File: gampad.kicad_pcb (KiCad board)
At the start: 2 copper layers, 18 parts, among them J1 swd header, U1 STM32L442KCUx, U2 MIC5504-3.3YM5

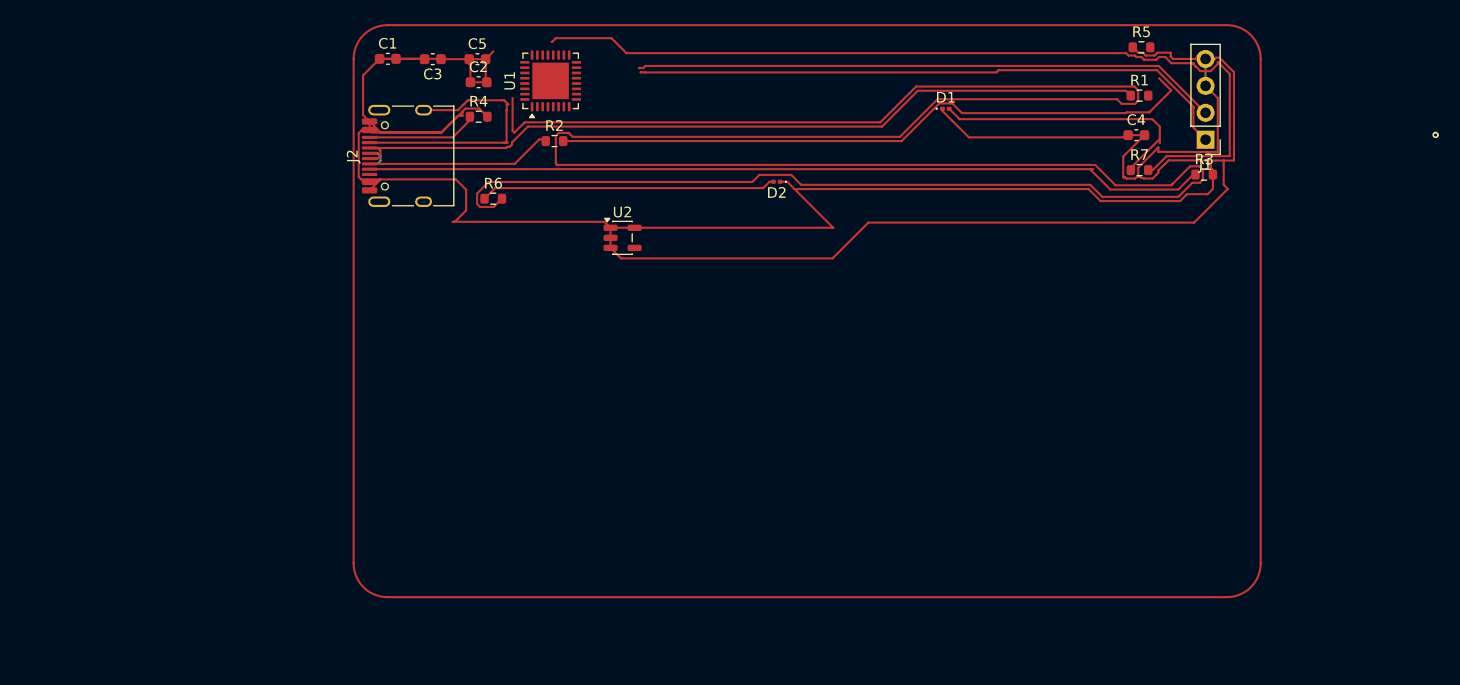
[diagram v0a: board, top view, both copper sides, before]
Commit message: WAHHHHHH tbh ddint edit much but deleted a bunch of useless files
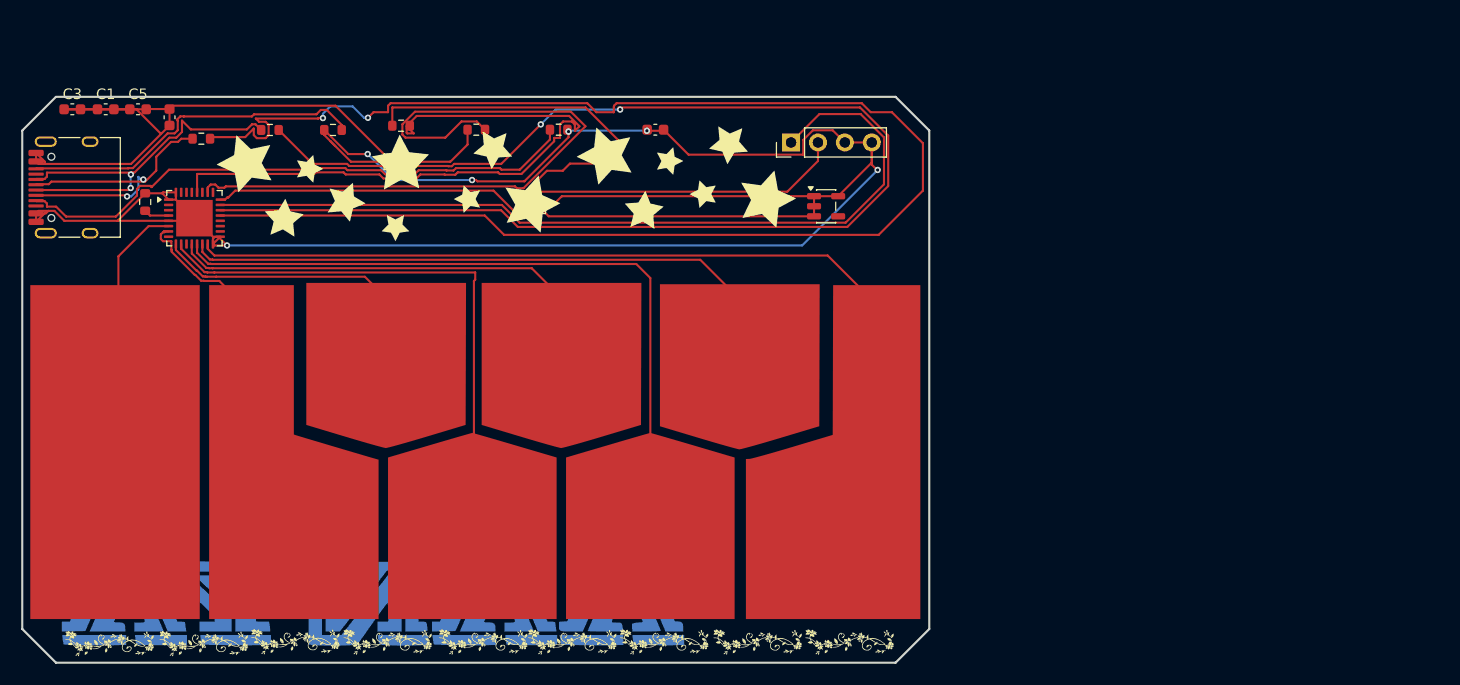
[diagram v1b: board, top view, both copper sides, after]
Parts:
- added G***: LOGO, LOGO, F.Cu at (114.7, 112.0)
- added G***: LOGO, LOGO, F.Cu at (86.4, 69.1)
- added G***: LOGO, LOGO, F.Cu at (79.9, 112.1)
- added G***: LOGO, LOGO, F.Cu at (130.5, 68.7)
- added G***: LOGO, LOGO, F.Cu at (120.4, 68.3)
- added G***: LOGO, LOGO, F.Cu at (123.4, 112.0)
- added G***: LOGO, LOGO, B.Cu at (104.6, 90.1)
- added G***: LOGO, LOGO, B.Cu at (95.9, 132.2)
- added G***: LOGO, LOGO, F.Cu at (71.0, 112.1)
- added G***: LOGO, LOGO, F.Cu at (96.6, 69.8)
- added G***: LOGO, LOGO, F.Cu at (140.9, 112.0)
- added G***: LOGO, LOGO, F.Cu at (132.2, 112.0)
- added G***: LOGO, LOGO, F.Cu at (88.6, 112.0)
- added G***: LOGO, LOGO, F.Cu at (108.2, 69.1)
- added G***: LOGO, LOGO, F.Cu at (106.3, 112.0)
- added G***: LOGO, LOGO, F.Cu at (97.3, 112.0)
- added J10: Conn_01x01, Connector_Pin:key5, F.Cu at (139.3, 94.4)
- added J3: Conn_01x01, Connector_Pin:key1, F.Cu at (80.3, 94.4)
- added J4: Conn_01x01, Connector_Pin:key2, F.Cu at (104.1, 94.4)
- added J5: Conn_01x01, Connector_Pin:key3, F.Cu at (104.6, 93.4)
- added J6: Conn_01x01, Connector_Pin:key4, F.Cu at (105.3, 94.4)
- added J7: Conn_01x01, Connector_Pin:key3, F.Cu at (121.2, 93.4)
- added J8: Conn_01x01, Connector_Pin:key4, F.Cu at (122.0, 94.4)
- added J9: Conn_01x01, Connector_Pin:key3, F.Cu at (138.0, 93.5)
- D1, D2: footprint LED_SMD:LED_0201_0603Metric -> LED_SMD:LED_0603_1608Metric
- moved R5 95.2 mm to (74.4, 70.8), turned to -90 degrees
- moved C4 91.3 mm to (76.7, 62.8), turned to 90 degrees
- moved R1 82.1 mm to (86.2, 64.0)
- moved R7 69.8 mm to (98.5, 63.6)
- moved R3 61.1 mm to (113.4, 64.0)
- moved D1 40.3 mm to (110.7, 71.2), turned to 180 degrees
- moved J1 39.1 mm to (135.3, 65.2), turned to 90 degrees
- moved U1 36.0 mm to (79.0, 72.3), turned to 0 degrees
- moved D2 35.6 mm to (98.4, 67.0), turned to 0 degrees
- moved C3 34.3 mm to (67.5, 62.0), turned to 0 degrees
- moved R2 33.3 mm to (79.7, 64.8)
- moved C5 32.4 mm to (73.7, 62.0)
- moved J2 31.6 mm to (68.1, 69.4)
- moved C1 27.0 mm to (70.7, 62.0)
- moved U2 19.4 mm to (138.6, 71.2)
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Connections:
- net Net-(J2-DN1) renamed /dn
- net Net-(J2-DP1) renamed /dp
- U1 pad 10: /key 4 -> key_4
- U1 pad 12: /key 5 -> key_5
- U1 pad 13: /key 6 -> key_6
- U1 pad 14: /key 7 -> key_7
- U1 pad 15: /key 8 -> key_8
- U1 pad 6: /key 1 -> key_1
- U1 pad 7: /key 2 -> key_2
- U1 pad 9: /key 3 -> key_3
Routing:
- net Net-(U1-PB3): track 263.0 -> 67.1 mm
- net pa12: track 0.00 -> 133.7 mm, vias 0 -> 2
- net pa11: track 61.7 -> 150.1 mm, vias 0 -> 2
- net key_8: track 0.00 -> 66.4 mm
- net key_6: track 0.00 -> 61.0 mm
- net key_7: track 0.00 -> 53.3 mm
- net key_4: track 0.00 -> 46.2 mm
- net /dp: track 77.1 -> 35.6 mm, vias 0 -> 2
- net key_5: track 0.00 -> 37.5 mm
- net (no net): track 25.6 -> 0.00 mm, vias 1 -> 0
- net Net-(J2-CC1): track 79.6 -> 54.5 mm
- net in/ou: track 57.3 -> 80.0 mm
- net Net-(J2-CC2): track 10.6 -> 32.9 mm
- net key_3: track 0.00 -> 22.3 mm
- net Net-(U1-PB5): track 82.7 -> 61.7 mm
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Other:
- board outline added: 85.6 x 53.4 mm

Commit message: heheh
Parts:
- removed the G*** at (95.9, 132.2)
